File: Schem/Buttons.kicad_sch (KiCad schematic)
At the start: 86 parts, among them SW1 SYNC_1, SW10 BEAT_JUMP_1, SW11 SAMPLER_1, SW12 SYNC_2, SW13 PLAY_2, SW14 CUE_2, SW15 LOOP_IN_2, SW16 LOOP_OUT_2, SW17 LOOP_ON_2, SW18 HOT_CUE_2, SW19 PAD_FX_2, SW2 PLAY_1, SW20 BEAT_JUMP_2, SW21 SAMPLER_2, SW22 CH1_CUE, SW23 CH2_CUE, SW24 MIC_ON, SW25 FX_ON, SW26 SMART_FADER_AUTO, SW27 BEAT_FX_NEG, SW28 BEAT_FX_POS, SW29 PAD1, SW3 CUE_1, SW30 PAD2, SW31 PAD3, SW32 PAD4, SW33 PAD5, SW34 PAD6, SW35 PAD7, SW36 PAD8, SW37 PAD9, SW38 PAD10, SW39 PAD11, SW4 LOOP_IN_1, SW40 PAD12, SW41 PAD13, SW42 PAD14, SW43 PAD15, SW44 PAD16, SW6 LOOP_OUT_1, SW7 LOOP_ON_1, SW8 HOT_CUE_1, SW9 PAD_FX_1

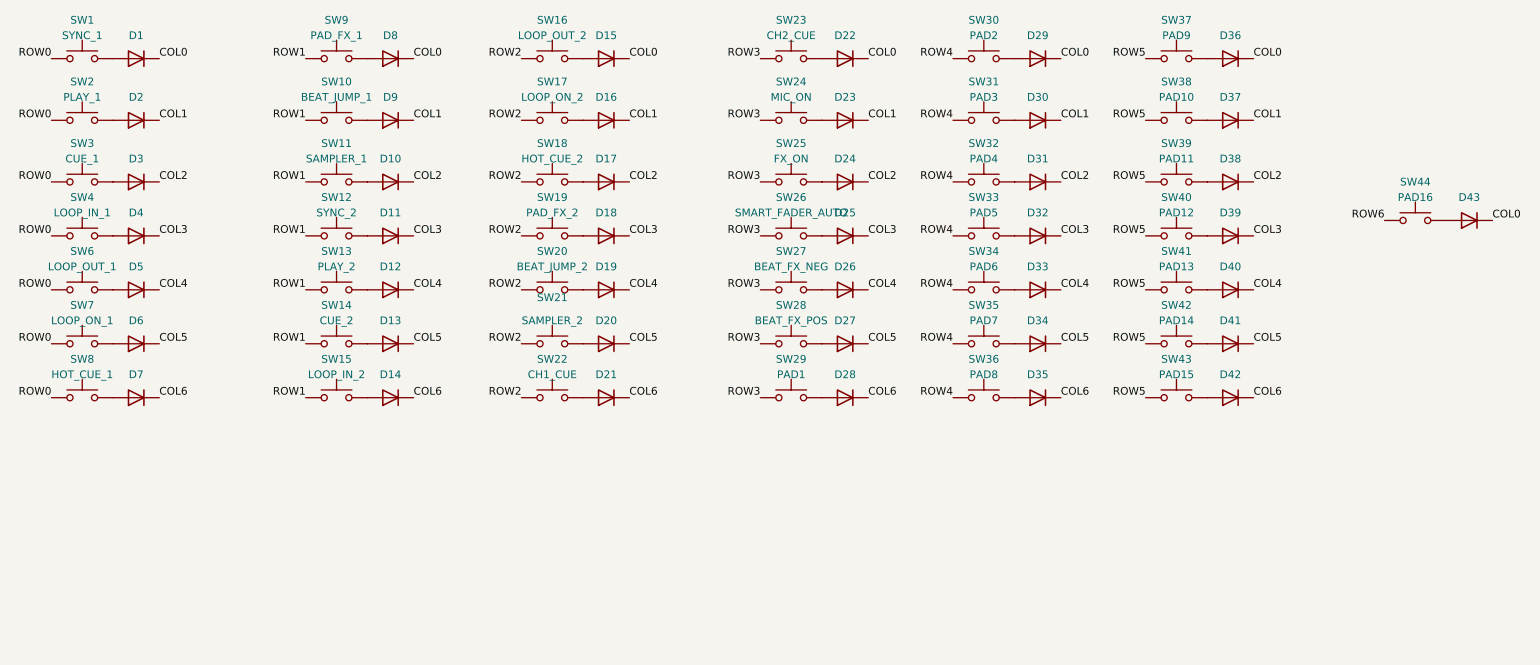
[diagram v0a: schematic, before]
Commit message: Update Schematic fixing errors (consult journal)
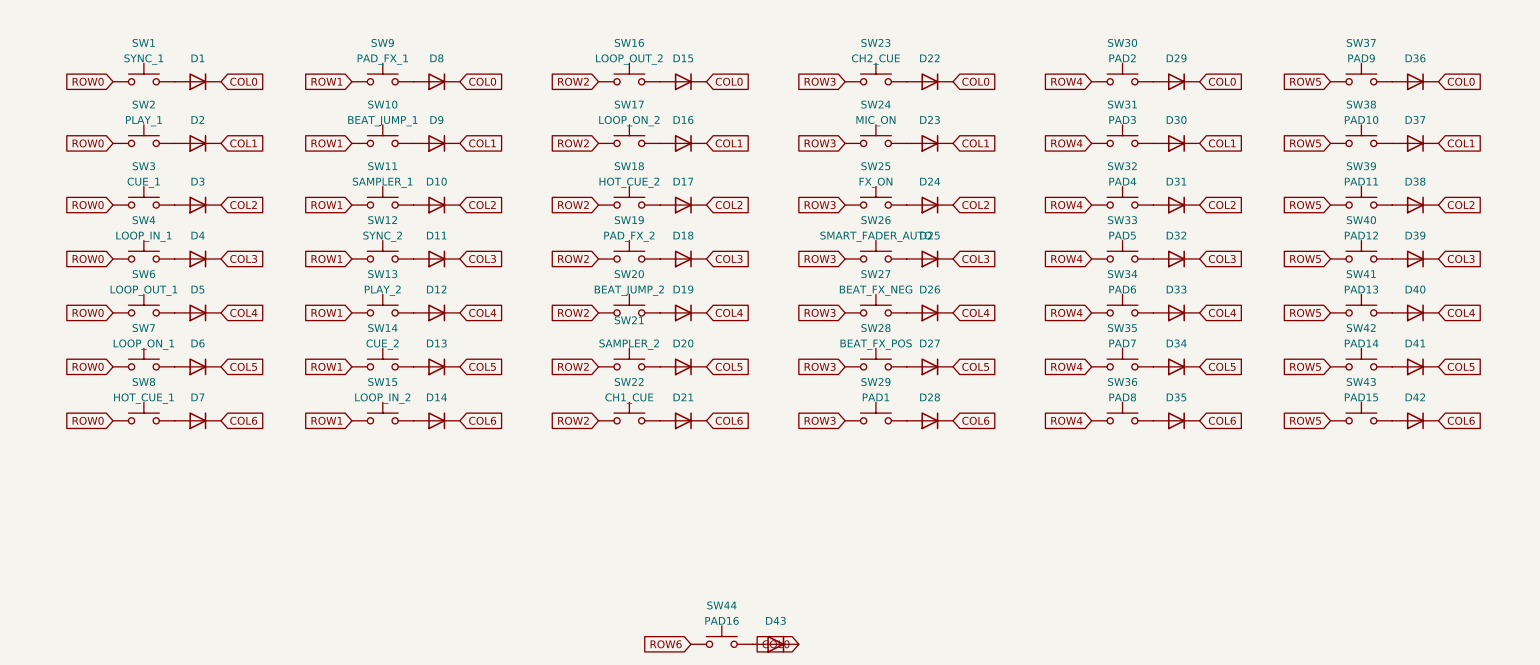
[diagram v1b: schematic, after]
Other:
- moved on the sheet: D1, D10, D11, D12, D13, D14, D15, D16, D17, D18, D19, D2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
